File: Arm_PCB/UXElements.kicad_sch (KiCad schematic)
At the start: 1 part

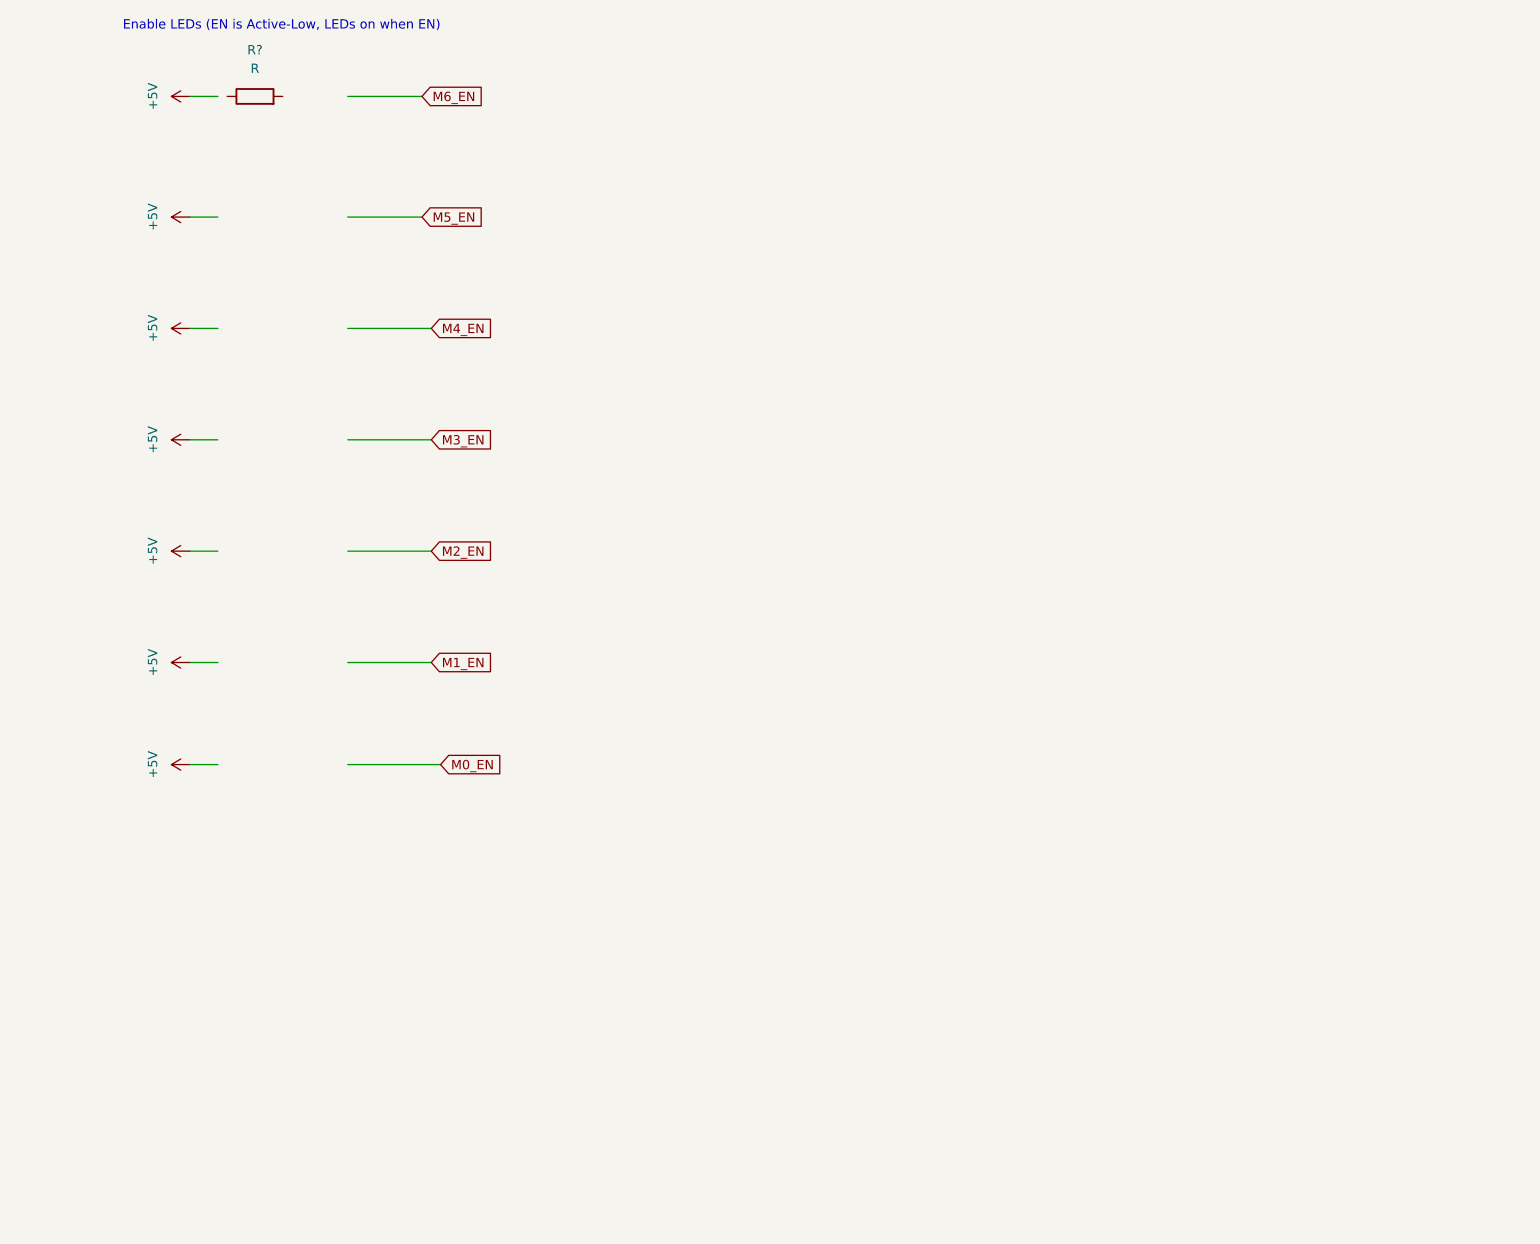
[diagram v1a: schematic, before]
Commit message: Changes, including UX and breakout pins
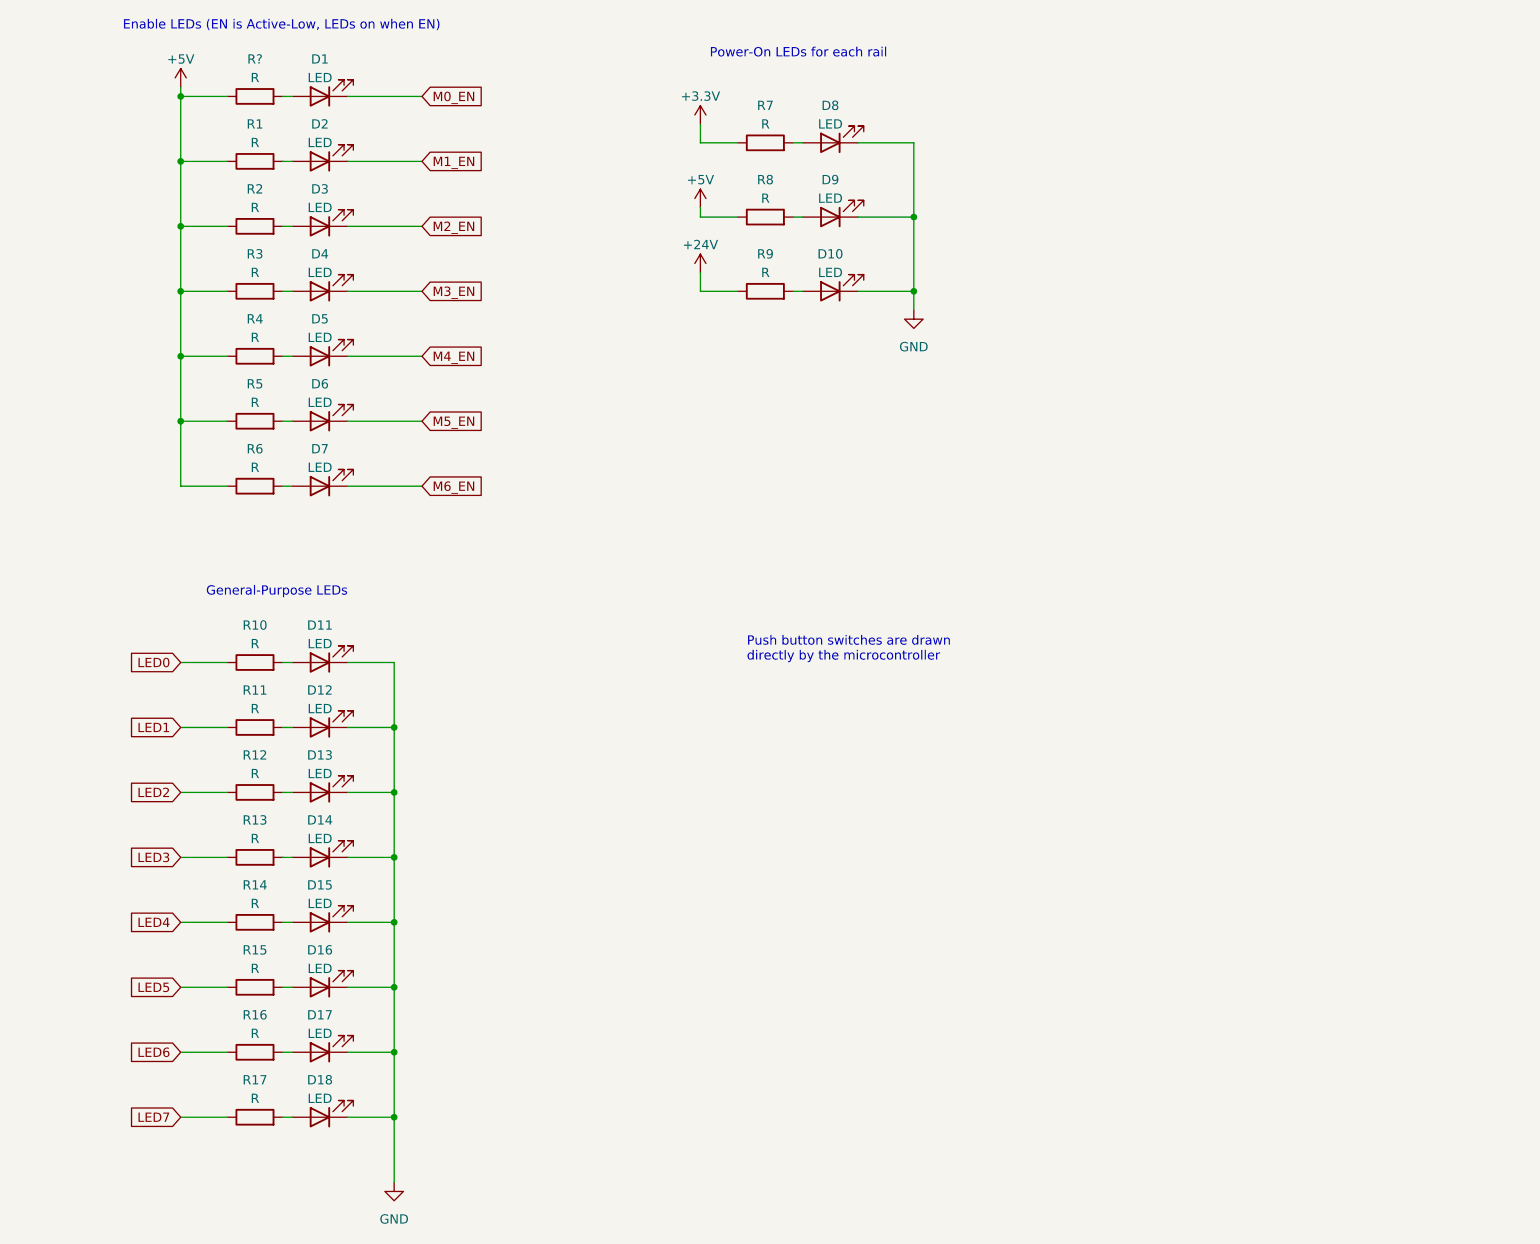
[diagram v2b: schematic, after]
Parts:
- added D1, D10, D11, D12, D13, D14, D15, D16, D17, D18, D2, D3, D4, D5, D6, D7, D8, D9: LED, symbol Device:LED
- added R1, R10, R11, R12, R13, R14, R15, R16, R17, R2, R3, R4, R5, R6, R7, R8, R9: R, symbol Device:R
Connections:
- net +5V: now also R?.1, R1.1, R2.1, R3.1, R4.1, R5.1, R6.1, R8.1
- net M0_EN: now also D1.1 (K)
- net M1_EN: now also D2.1 (K)
- net M2_EN: now also D3.1 (K)
- net M3_EN: now also D4.1 (K)
- net M4_EN: now also D5.1 (K)
- net M5_EN: now also D6.1 (K)
- net M6_EN: now also D7.1 (K)
- net at R?.2: now also D1.2 (A)
- new net: D17.2 (A), R16.2
- new net: D3.2 (A), R2.2
- new net: D12.2 (A), R11.2
- new net: D15.2 (A), R14.2
- new net: D16.2 (A), R15.2
- new net: D13.2 (A), R12.2
- new net: D6.2 (A), R5.2
- new net: D11.2 (A), R10.2
- new net: D7.2 (A), R6.2
- new net: D9.2 (A), R8.2
- new net: D2.2 (A), R1.2
- new net: D10.2 (A), R9.2
- new net: D4.2 (A), R3.2
- new net: D18.2 (A), R17.2
- new net: D14.2 (A), R13.2
- new net: D8.2 (A), R7.2
- new net: D5.2 (A), R4.2
- new net +24V: R9.1
- new net +3.3V: R7.1
- new net GND: D10.1 (K), D11.1 (K), D12.1 (K), D13.1 (K), D14.1 (K), D15.1 (K), D16.1 (K), D17.1 (K), D18.1 (K), D8.1 (K), D9.1 (K)
- new net LED0: R10.1
- new net LED1: R11.1
- new net LED2: R12.1
- new net LED3: R13.1
- new net LED4: R14.1
- new net LED5: R15.1
- new net LED6: R16.1
- new net LED7: R17.1
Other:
- note added: "General-Purpose LEDs"
- note added: "Power-On LEDs for each rail"
- note added: "Push button switches are drawn directly by the microcontroller"

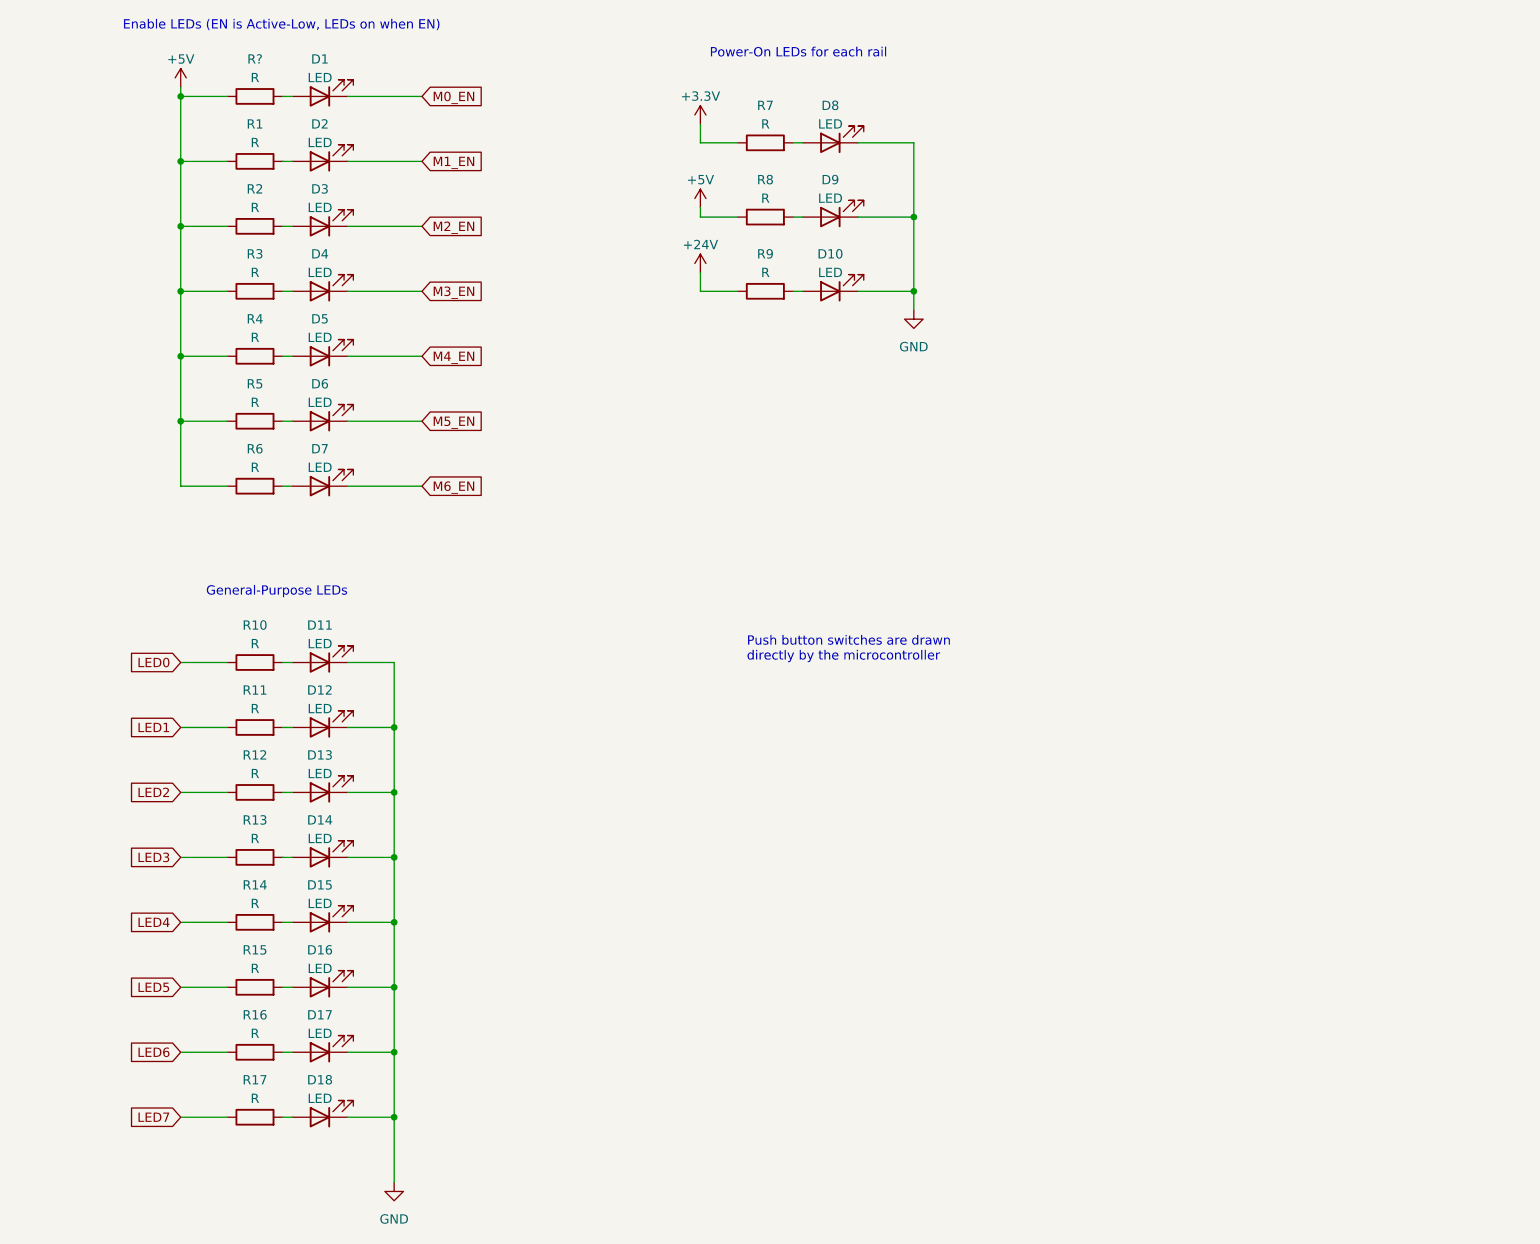
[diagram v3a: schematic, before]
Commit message: Annotate all pages
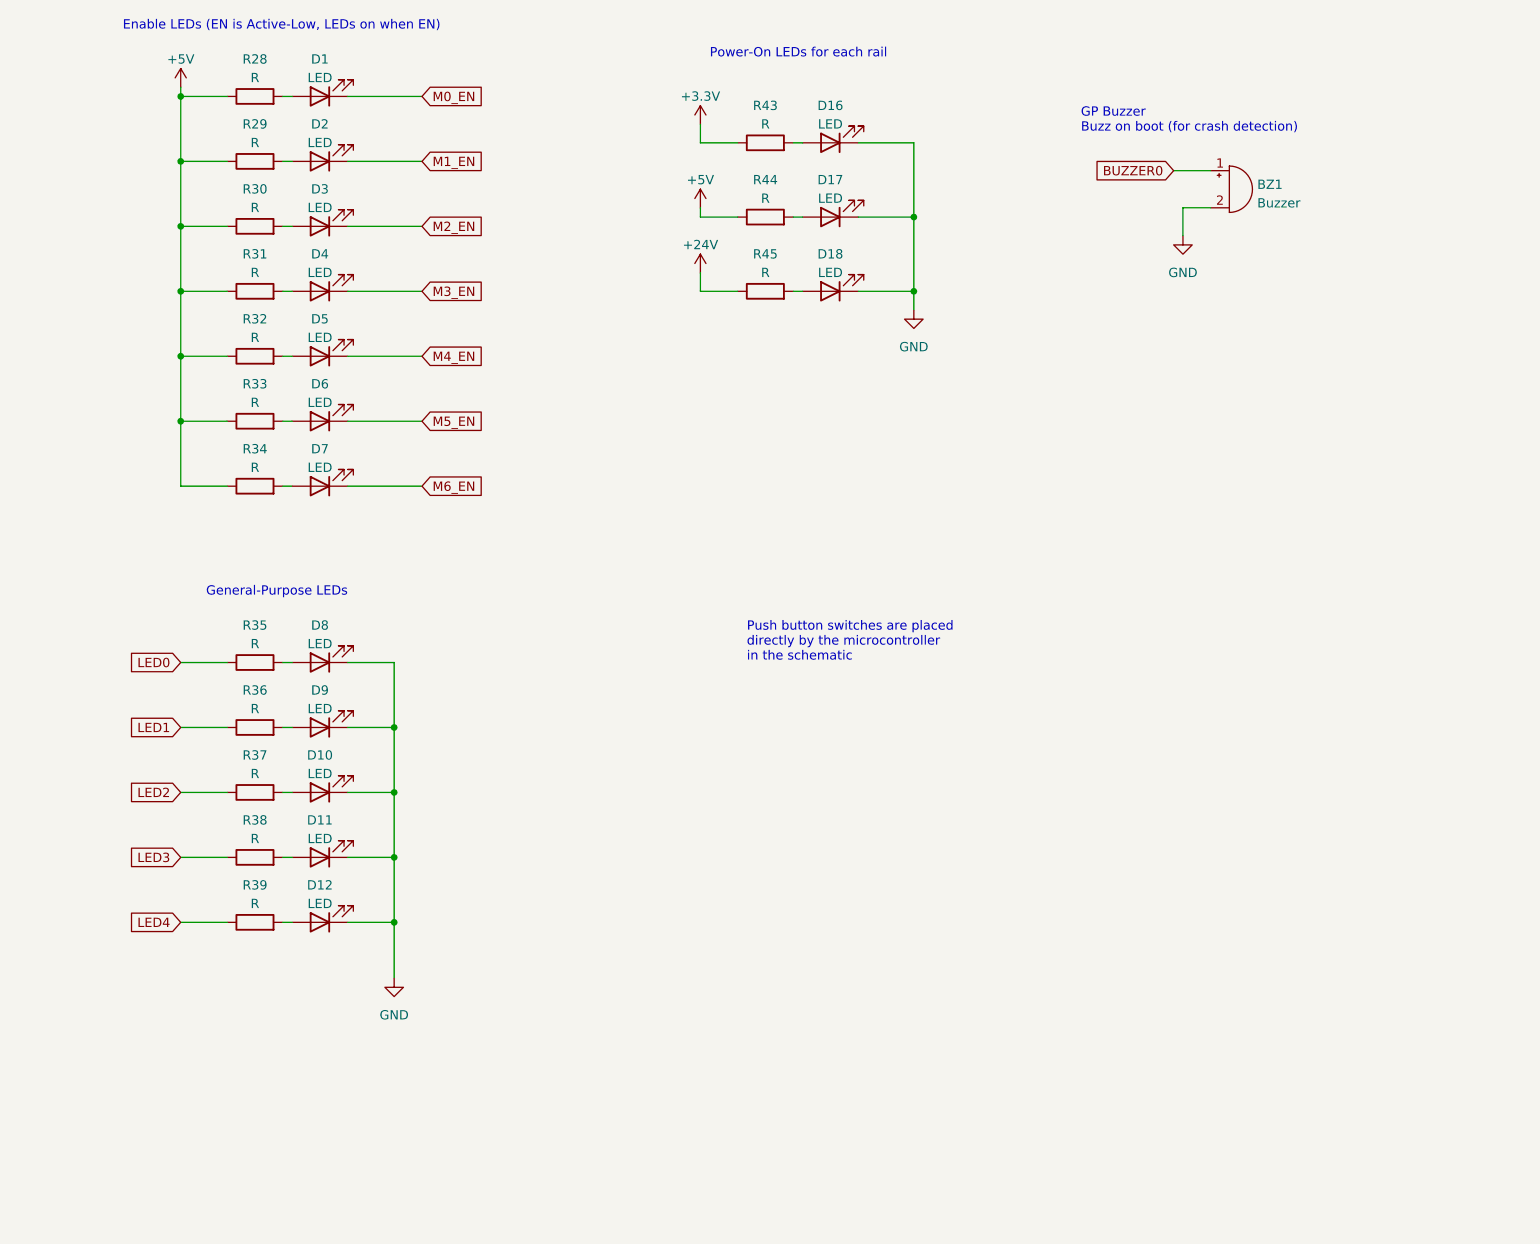
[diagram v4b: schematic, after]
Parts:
- removed D16, D17, D18: LED, symbol Device:LED
- removed R15, R16, R17: R, symbol Device:R
- added BZ1: Buzzer, symbol Device:Buzzer
- gave numbers to parts that had none: 1
- renumbered D13 to D10, D14 to D11, D15 to D12, D8 to D16, D9 to D17, D10 to D18, D11 to D8, D12 to D9, R1 to R29, R2 to R30, R3 to R31, R4 to R32, R5 to R33, R6 to R34, R10 to R35, R11 to R36, R12 to R37, R13 to R38, R14 to R39, R7 to R43, R8 to R44, R9 to R45
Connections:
- net GND: now also BZ1.2 (+)
- new net BUZZER0: BZ1.1 (-)
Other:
- note added: "GP Buzzer Buzz on boot (for crash detection)"
- note added: "Push button switches are placed directly by the microcontroller in the schematic"
- note removed: "Push button switches are drawn directly by the microcontroller"
